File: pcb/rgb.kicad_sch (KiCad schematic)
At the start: 47 parts, among them J1 2.54-2*8P, J3 B4PS-VH, J4 TYPE-C-31-M-12, J5 TF-01A, J6 V_BATT, J7 B4PS-VH, SW1 MS-22C01-G010, U11 RV-3028-C7, U4 EVQQ2, U5 ESP32-WROOM-32E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

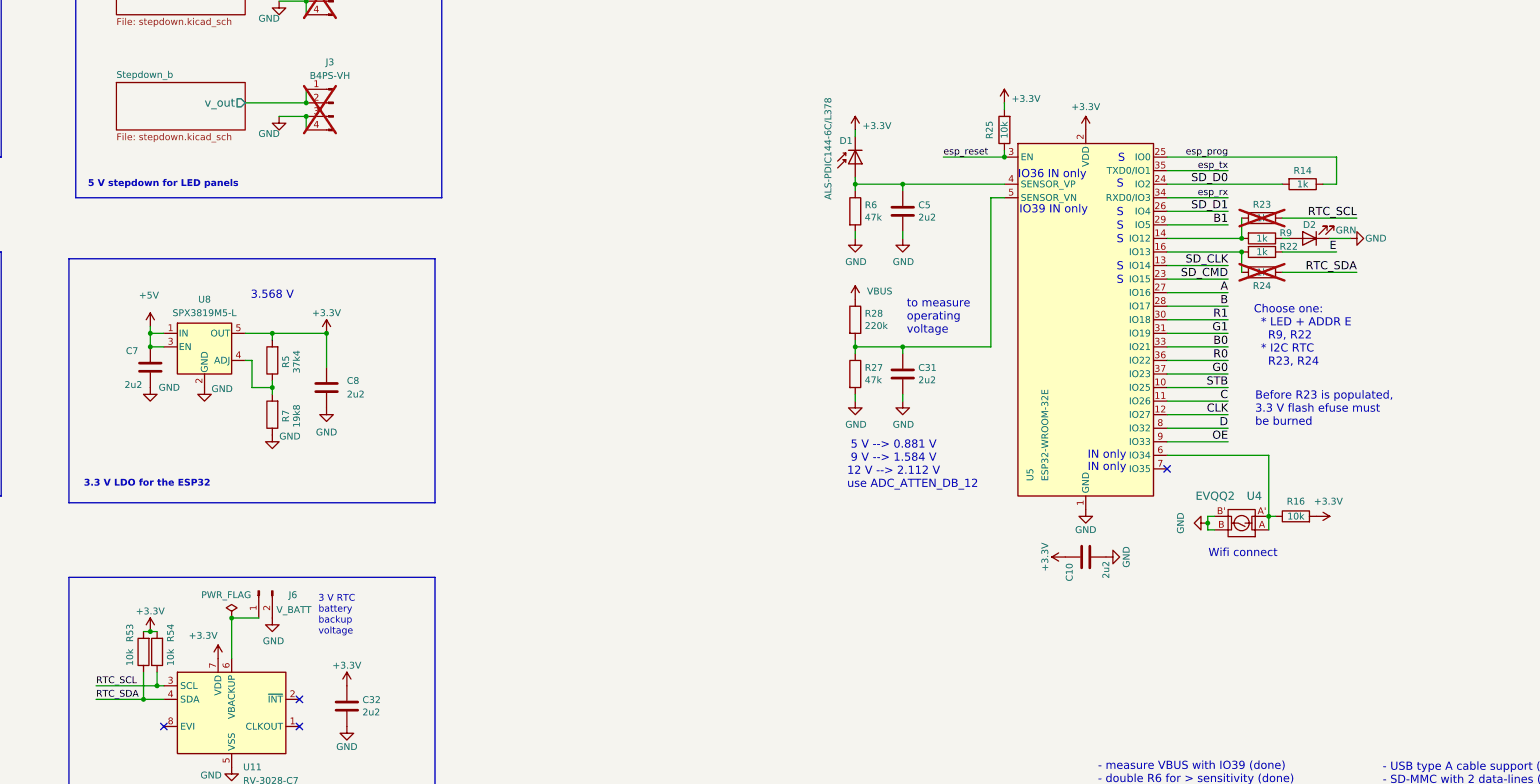
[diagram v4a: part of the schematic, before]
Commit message: rev3 routing complete
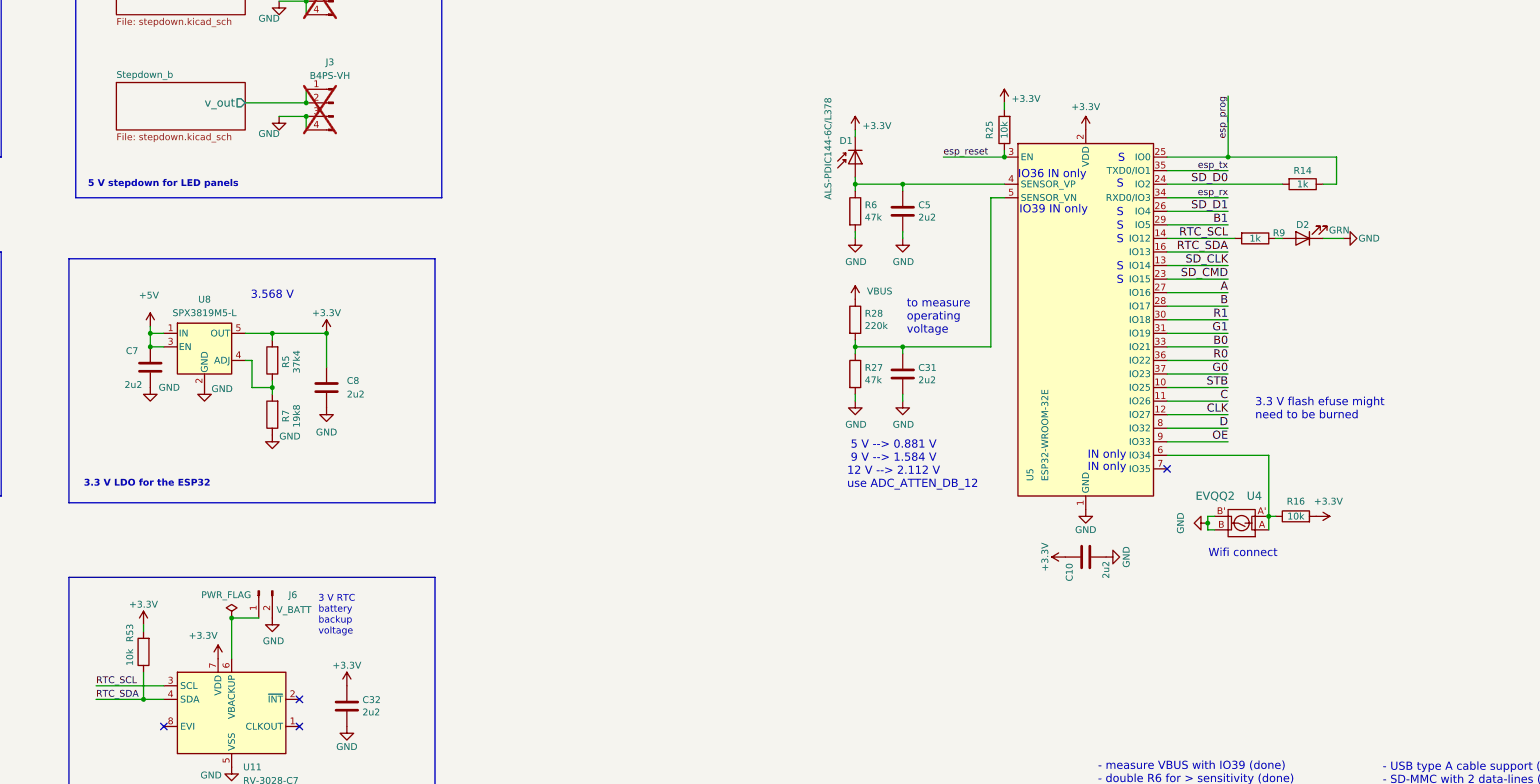
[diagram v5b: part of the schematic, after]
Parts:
- removed R22, R23, R24: 1k, Resistor_SMD:R_0603_1608Metric, symbol Device:R
- removed R54: 10k, Resistor_SMD:R_0603_1608Metric, symbol Device:R
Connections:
- net RTC_SCL: now also R9.2, U5.14 (IO12)
- net RTC_SDA: now also U5.16 (IO13)
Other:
- note added: "3.3 V flash efuse might need to be burned"
- note removed: "Before R23 is populated, 3.3 V flash efuse must be burned"
- note removed: "Choose one: * LED + ADDR E R9, R22 * I2C RTC R23, R24"
- moved on the sheet: D2, R9

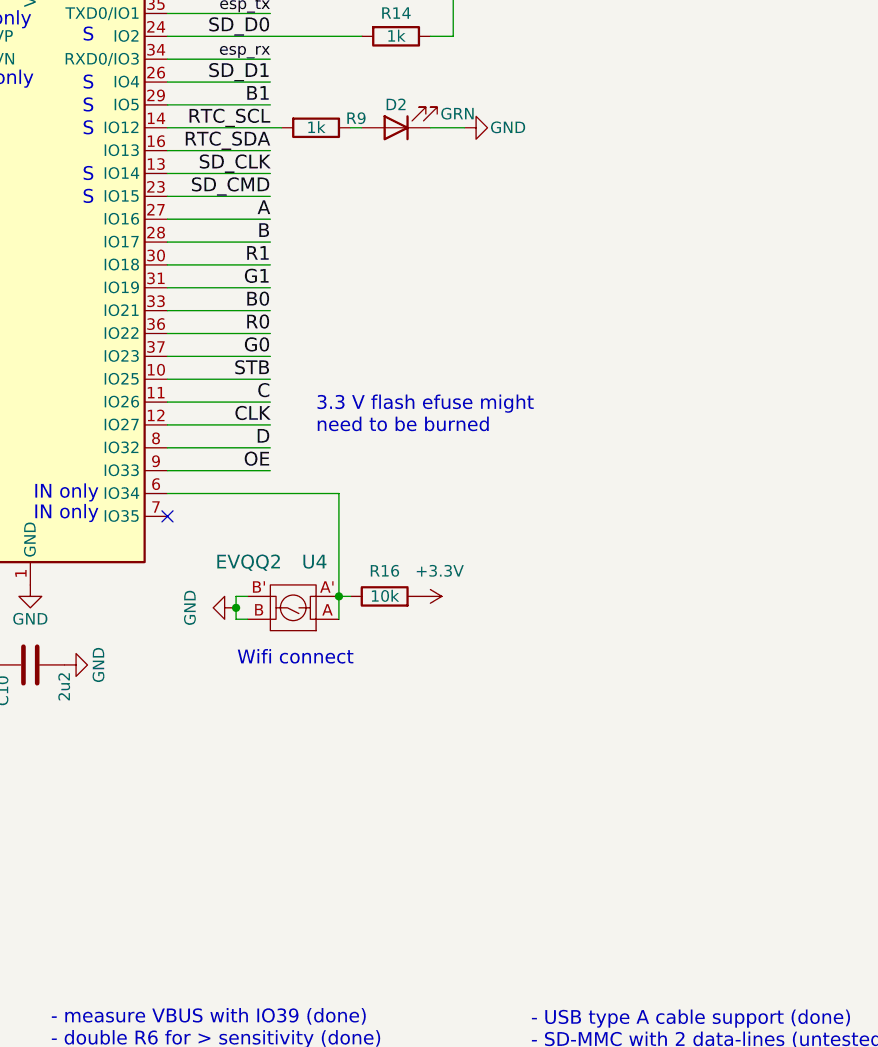
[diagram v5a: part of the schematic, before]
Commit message: rev3 pcb: add IR receiver
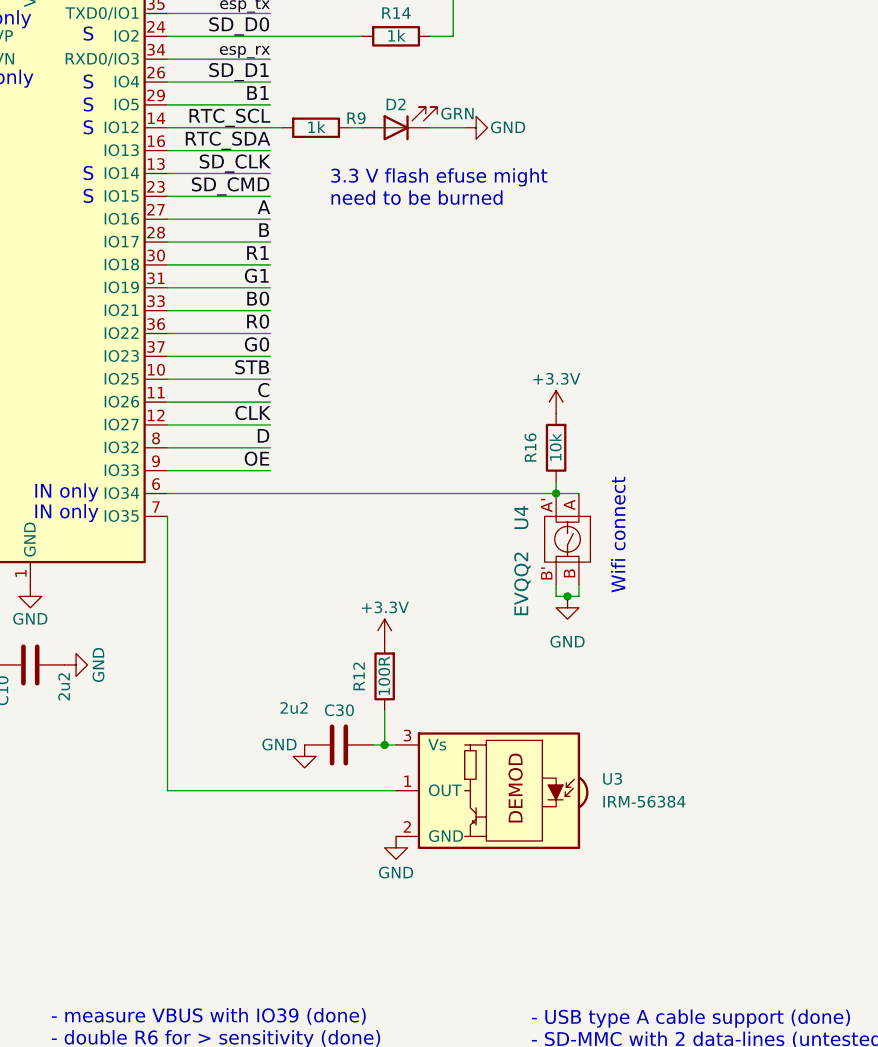
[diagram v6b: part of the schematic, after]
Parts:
- added C30: 2u2, Capacitor_SMD:C_0603_1608Metric, symbol Device:C
- added R12: 100R, Resistor_SMD:R_0603_1608Metric, symbol Device:R
- added U3: IRM-56384, OptoDevice:Vishay_MOLD-3Pin, symbol Interface_Optical:TSDP341xx
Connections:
- net +3.3V: now also R12.2
- net GND: now also C30.1, U3.2 (GND)
- net at U5.7 (IO35): now also U3.1 (OUT)
- new net: C30.2, R12.1, U3.3 (Vs)
- no-connect marks 15 -> 14
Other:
- moved on the sheet: R16, U4

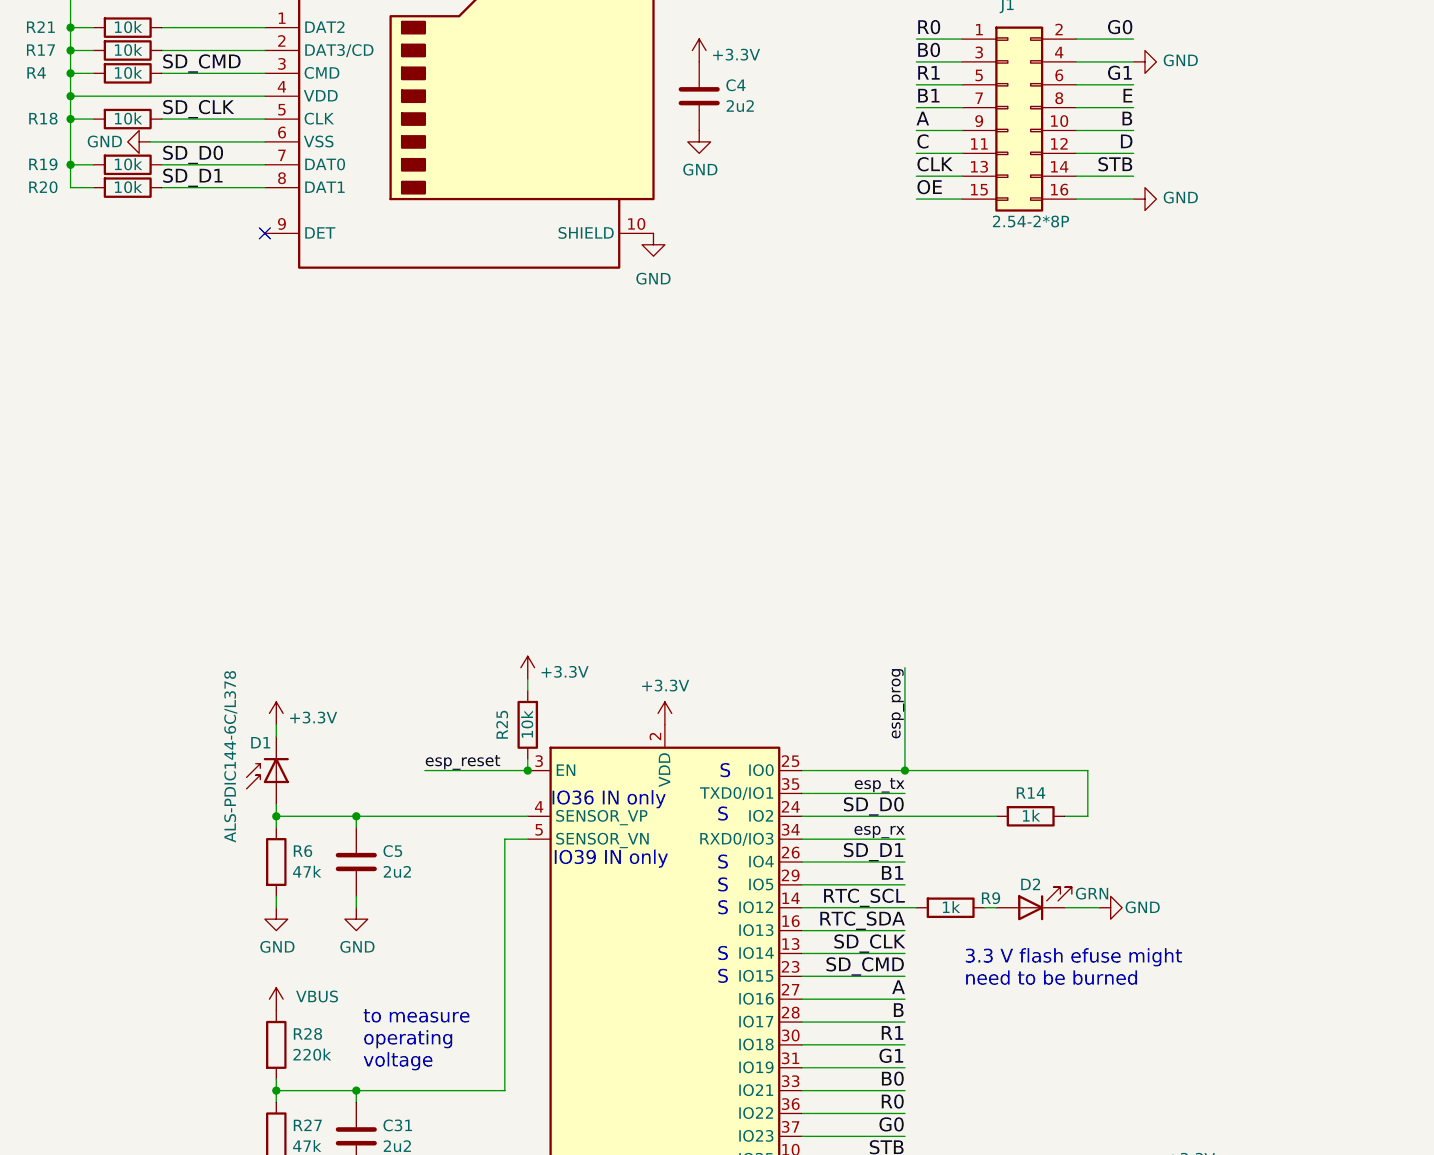
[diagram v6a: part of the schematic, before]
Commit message: pcb: remove D1 data pin from SD card
  * 2 wire MMC mode does not exist. Can only use 1 wire anyway.
  * Use the freed up GPIO for address line E
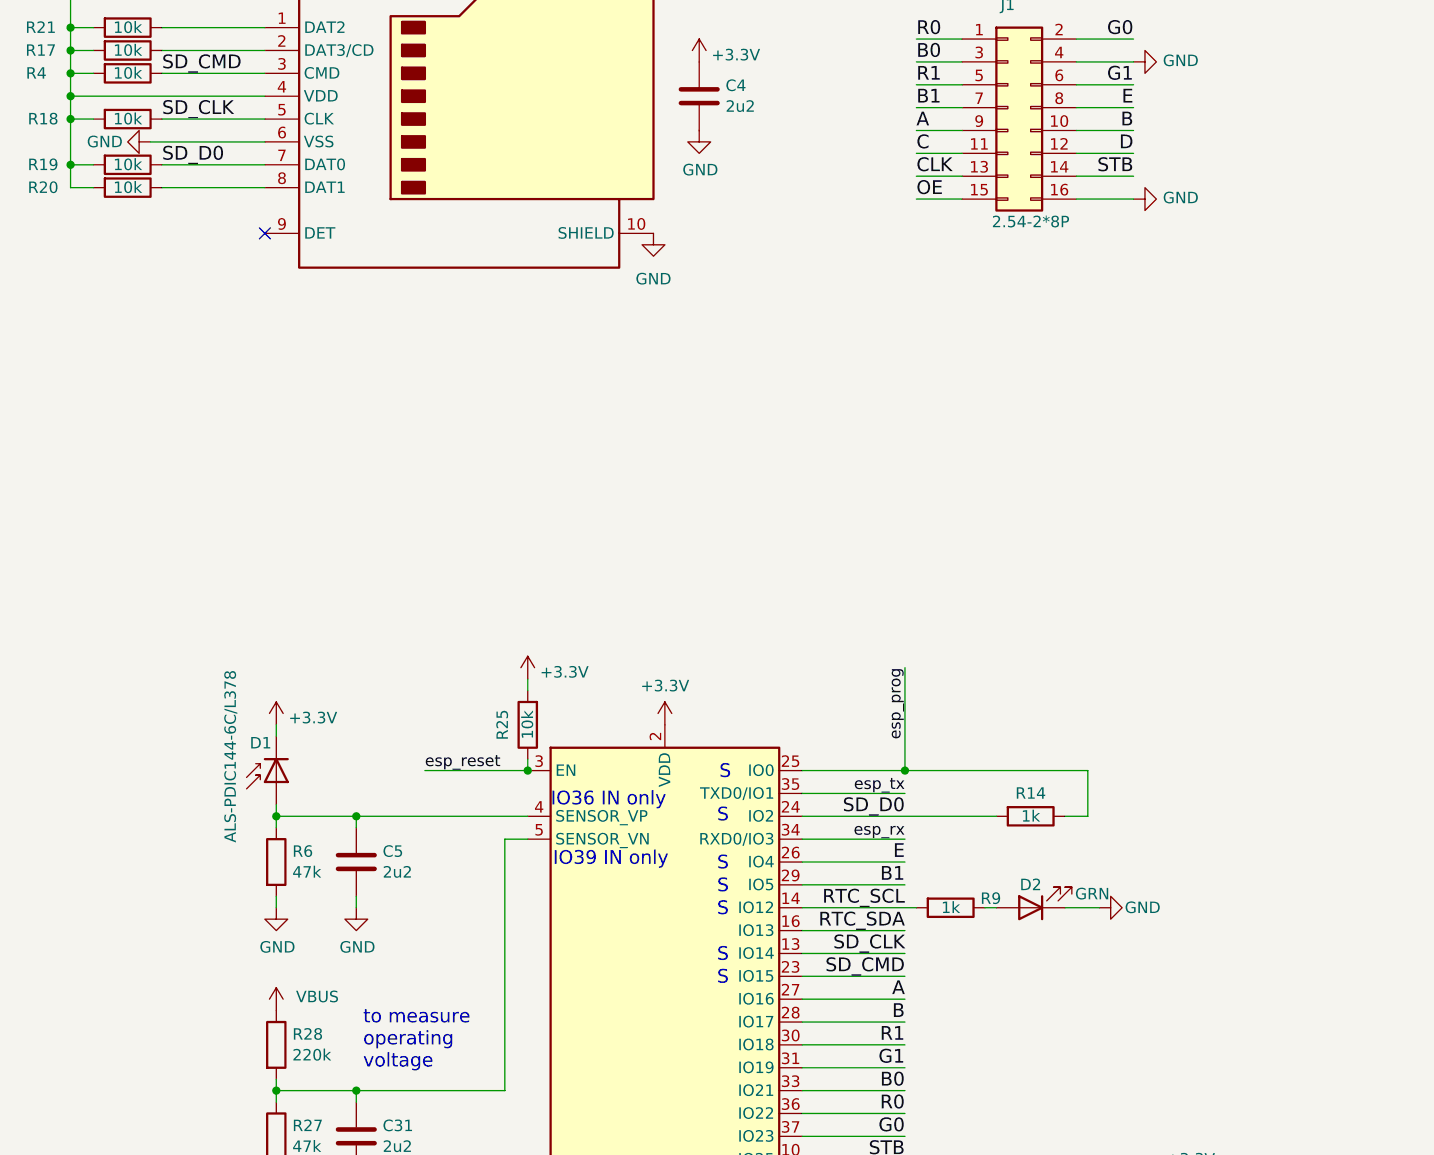
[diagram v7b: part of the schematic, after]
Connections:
- net E: now also U5.26 (IO4)
- net SD_D1: no longer names the net of J5.8 (DAT1), R20.1
- net SD_D1: no longer U5.26 (IO4)
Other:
- note removed: "3.3 V flash efuse might need to be burned"
